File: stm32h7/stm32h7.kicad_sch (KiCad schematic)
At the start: 23 parts, among them J1 Conn_02x18_Counter_Clockwise, J2 Conn_02x18_Counter_Clockwise, J3 Conn_02x18_Counter_Clockwise, J4 Conn_02x18_Counter_Clockwise, SW1 SW_SPDT, U1 STM32H743ZITx, Y1 ABM3-8.000MHZ

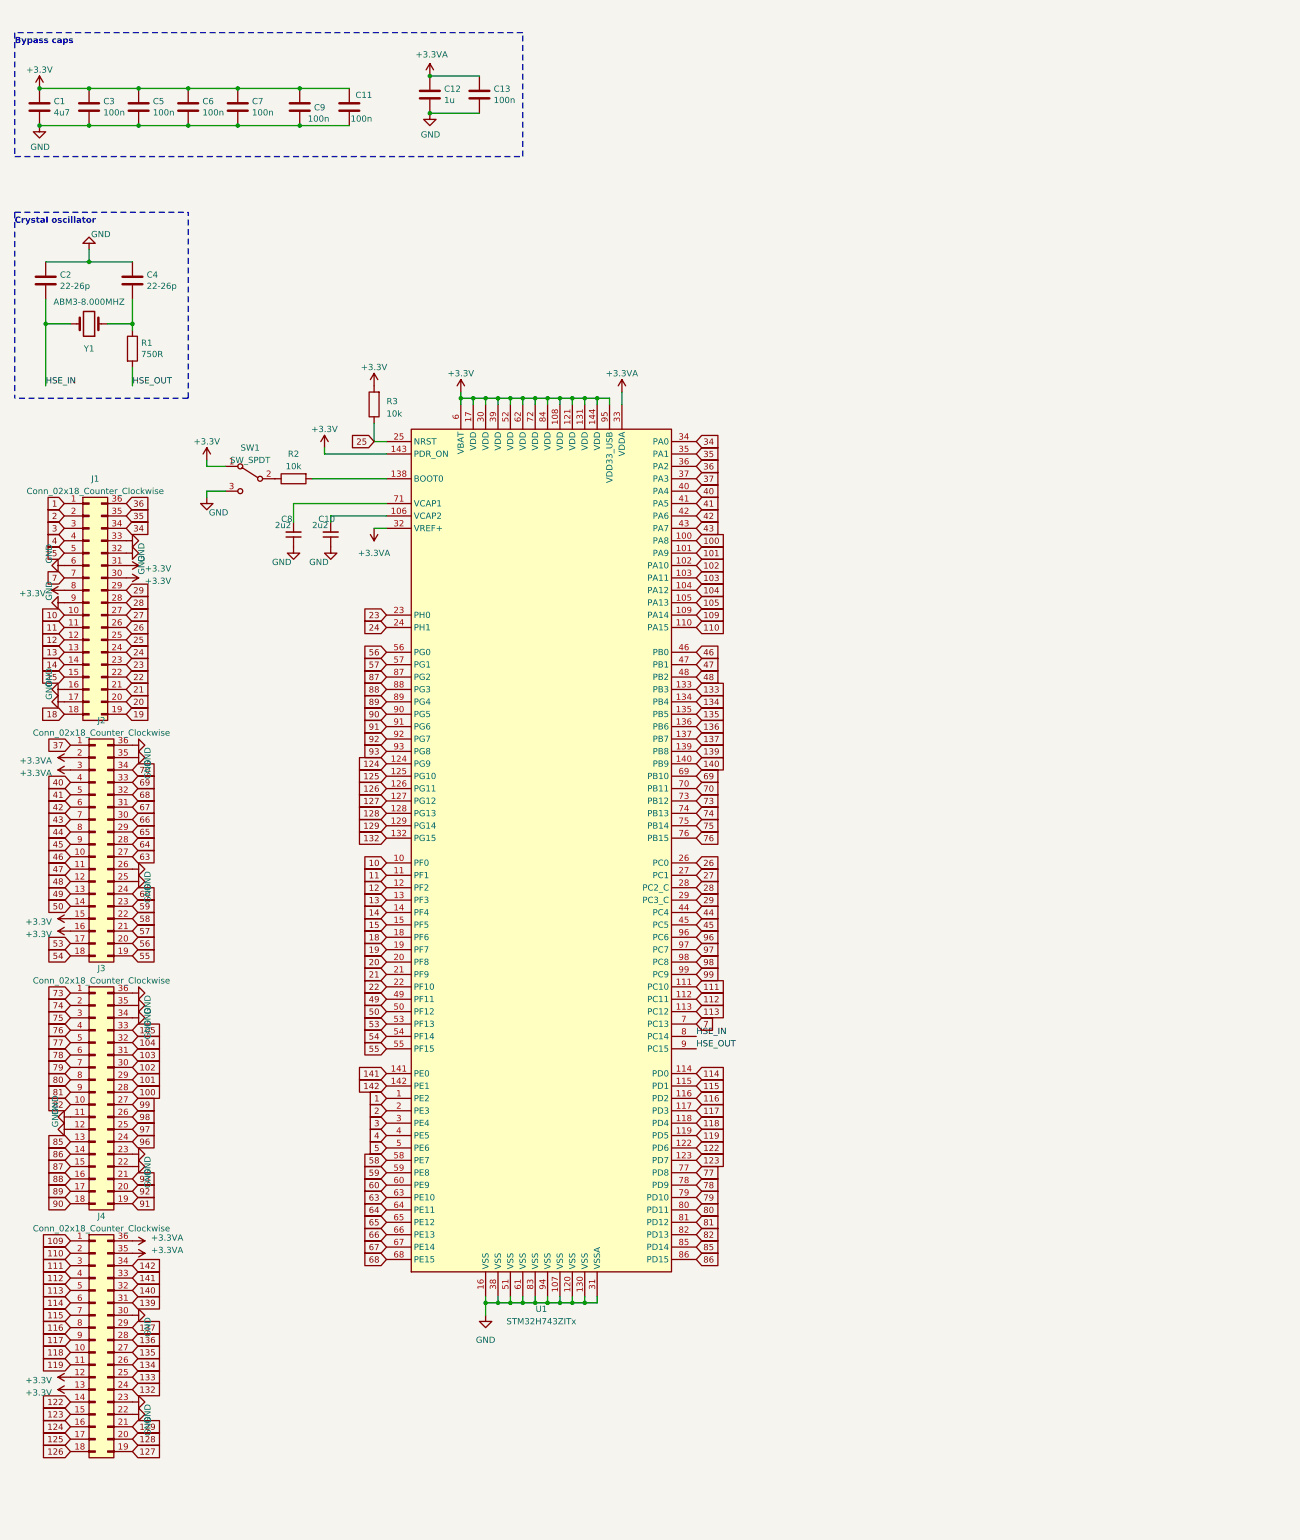
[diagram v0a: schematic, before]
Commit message: add gerber for stm32h7
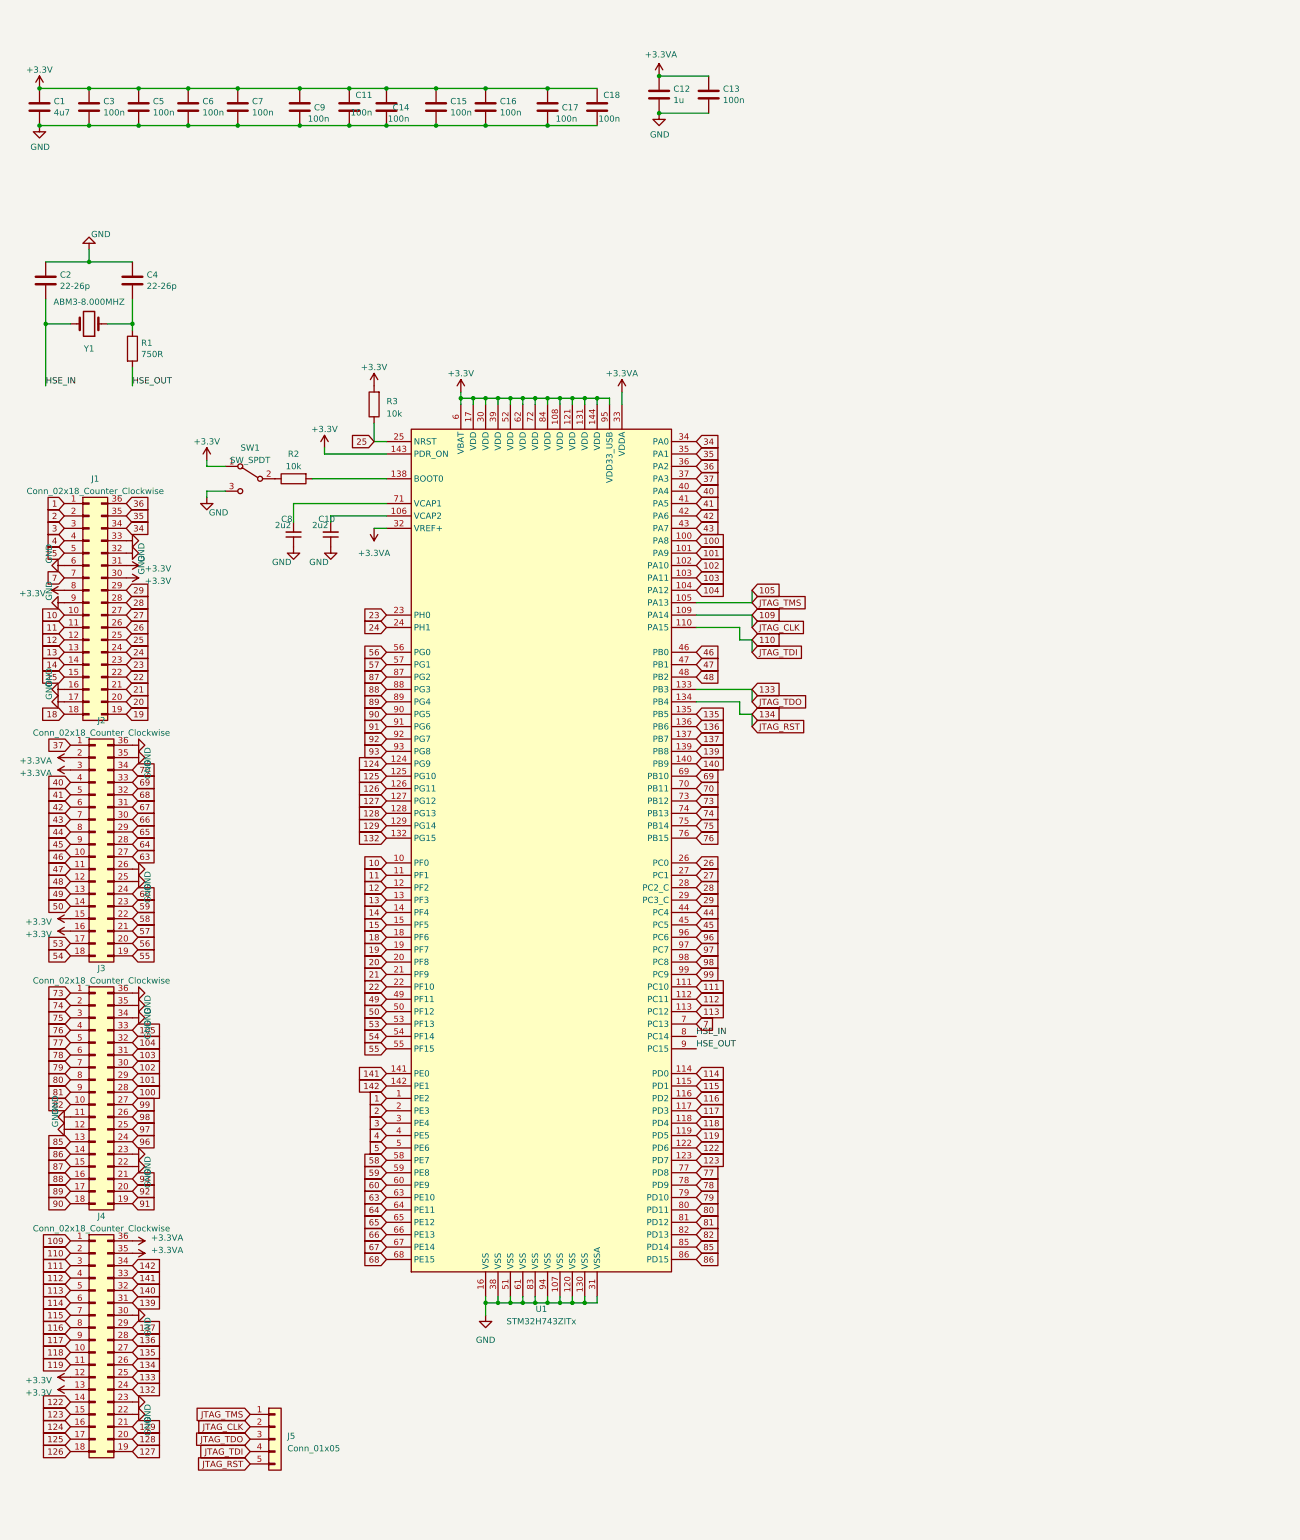
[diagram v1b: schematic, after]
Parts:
- added C14, C15, C16, C17, C18: 100n, Capacitor_SMD:C_0603_1608Metric, symbol Device:C
- added J5: Conn_01x05, Connector_PinHeader_2.00mm:PinHeader_1x05_P2.00mm_Vertical, symbol Connector_Generic:Conn_01x05
- C10, C8: LCSC (none) -> C23630; LCSC Part # (none) -> C23630
- R2, R3: LCSC (none) -> C25804; LCSC Part # (none) -> C25804
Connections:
- net +3V3: now also C14.1, C15.1, C16.1, C17.1, C18.1
- net 105: now also J5.1 (Pin_1)
- net 109: now also J5.2 (Pin_2)
- net 110: now also J5.4 (Pin_4)
- net 133: now also J5.3 (Pin_3)
- net 134: now also J5.5 (Pin_5)
- net GND: now also C14.2, C15.2, C16.2, C17.2, C18.2
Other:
- note removed: "Bypass caps"
- note removed: "Crystal oscillator"
- moved on the sheet: C12, C13

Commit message: add dedicated symbol and footprint for easier porting
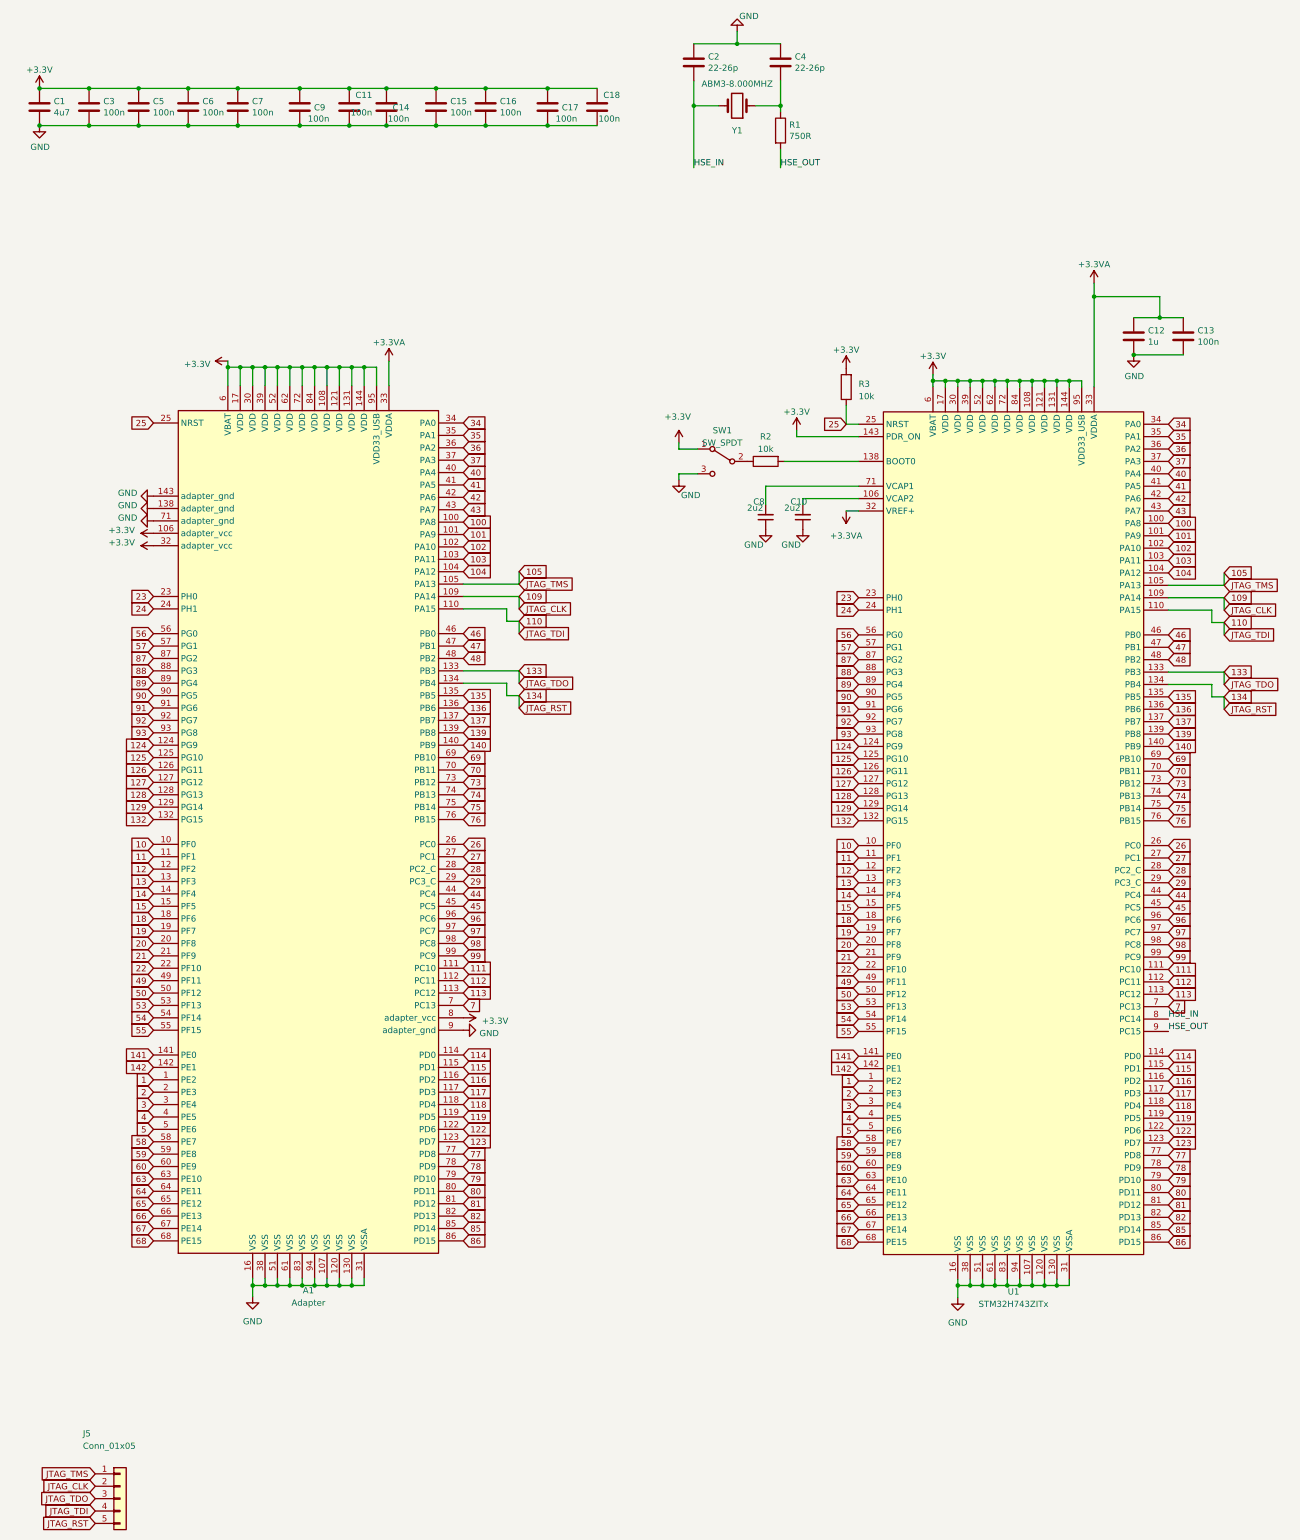
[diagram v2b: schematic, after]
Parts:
- removed J1, J2, J3, J4: Conn_02x18_Counter_Clockwise, Connector_PinHeader_2.00mm:PinHeader_2x18_P2.00mm_Vertical, symbol Connector_Generic:Conn_02x18_Counter_Clockwise
- added A1: Adapter, Connector_PinHeader_2.00mm:stm32h7_adapter, symbol MCU_ST_STM32H7:STM32H743ZITx
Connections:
- net +3.3VA: now also A1.33 (VDDA)
- net +3V3: now also A1.106 (adapter_vcc), A1.108 (VDD), A1.121 (VDD), A1.131 (VDD), A1.144 (VDD), A1.17 (VDD), A1.30 (VDD), A1.32 (adapter_vcc), A1.39 (VDD), A1.52 (VDD), A1.6 (VBAT), A1.62 (VDD), A1.72 (VDD), A1.8 (adapter_vcc), A1.84 (VDD), A1.95 (VDD33_USB)
- net 1: now also A1.1 (PE2)
- net 10: now also A1.10 (PF0)
- net 100: now also A1.100 (PA8)
- net 101: now also A1.101 (PA9)
- net 102: now also A1.102 (PA10)
- net 103: now also A1.103 (PA11)
- net 104: now also A1.104 (PA12)
- net 105: now also A1.105 (PA13)
- net 109: now also A1.109 (PA14)
- net 11: now also A1.11 (PF1)
- net 110: now also A1.110 (PA15)
- net 111: now also A1.111 (PC10)
- net 112: now also A1.112 (PC11)
- net 113: now also A1.113 (PC12)
- net 114: now also A1.114 (PD0)
- net 115: now also A1.115 (PD1)
- net 116: now also A1.116 (PD2)
- net 117: now also A1.117 (PD3)
- net 118: now also A1.118 (PD4)
- net 119: now also A1.119 (PD5)
- net 12: now also A1.12 (PF2)
- net 122: now also A1.122 (PD6)
- net 123: now also A1.123 (PD7)
- net 124: now also A1.124 (PG9)
- net 125: now also A1.125 (PG10)
- net 126: now also A1.126 (PG11)
- net 127: now also A1.127 (PG12)
- net 128: now also A1.128 (PG13)
- net 129: now also A1.129 (PG14)
- net 13: now also A1.13 (PF3)
- net 132: now also A1.132 (PG15)
- net 133: now also A1.133 (PB3)
- net 134: now also A1.134 (PB4)
- net 135: now also A1.135 (PB5)
- net 136: now also A1.136 (PB6)
- net 137: now also A1.137 (PB7)
- net 139: now also A1.139 (PB8)
- net 14: now also A1.14 (PF4)
- net 140: now also A1.140 (PB9)
- net 141: now also A1.141 (PE0)
- net 142: now also A1.142 (PE1)
- net 15: now also A1.15 (PF5)
- net 18: now also A1.18 (PF6)
- net 19: now also A1.19 (PF7)
- net 2: now also A1.2 (PE3)
- net 20: now also A1.20 (PF8)
- net 21: now also A1.21 (PF9)
- net 22: now also A1.22 (PF10)
- net 23: now also A1.23 (PH0)
- net 24: now also A1.24 (PH1)
- net 25: now also A1.25 (NRST)
- net 26: now also A1.26 (PC0)
- net 27: now also A1.27 (PC1)
- net 28: now also A1.28 (PC2_C)
- net 29: now also A1.29 (PC3_C)
- net 3: now also A1.3 (PE4)
- net 34: now also A1.34 (PA0)
- net 35: now also A1.35 (PA1)
- net 36: now also A1.36 (PA2)
- net 37: now also A1.37 (PA3)
- net 4: now also A1.4 (PE5)
- net 40: now also A1.40 (PA4)
- net 41: now also A1.41 (PA5)
- net 42: now also A1.42 (PA6)
- net 43: now also A1.43 (PA7)
- net 44: now also A1.44 (PC4)
- net 45: now also A1.45 (PC5)
- net 46: now also A1.46 (PB0)
- net 47: now also A1.47 (PB1)
- net 48: now also A1.48 (PB2)
- net 49: now also A1.49 (PF11)
- net 5: now also A1.5 (PE6)
- net 50: now also A1.50 (PF12)
- net 53: now also A1.53 (PF13)
- net 54: now also A1.54 (PF14)
- net 55: now also A1.55 (PF15)
- net 56: now also A1.56 (PG0)
- net 57: now also A1.57 (PG1)
- net 58: now also A1.58 (PE7)
- net 59: now also A1.59 (PE8)
- net 60: now also A1.60 (PE9)
- net 63: now also A1.63 (PE10)
- net 64: now also A1.64 (PE11)
- net 65: now also A1.65 (PE12)
- net 66: now also A1.66 (PE13)
- net 67: now also A1.67 (PE14)
- net 68: now also A1.68 (PE15)
- net 69: now also A1.69 (PB10)
- net 7: now also A1.7 (PC13)
- net 70: now also A1.70 (PB11)
- net 73: now also A1.73 (PB12)
- net 74: now also A1.74 (PB13)
- net 75: now also A1.75 (PB14)
- net 76: now also A1.76 (PB15)
- net 77: now also A1.77 (PD8)
- net 78: now also A1.78 (PD9)
- net 79: now also A1.79 (PD10)
- net 80: now also A1.80 (PD11)
- net 81: now also A1.81 (PD12)
- net 82: now also A1.82 (PD13)
- net 85: now also A1.85 (PD14)
- net 86: now also A1.86 (PD15)
- net 87: now also A1.87 (PG2)
- net 88: now also A1.88 (PG3)
- net 89: now also A1.89 (PG4)
- net 90: now also A1.90 (PG5)
- net 91: now also A1.91 (PG6)
- net 92: now also A1.92 (PG7)
- net 93: now also A1.93 (PG8)
- net 96: now also A1.96 (PC6)
- net 97: now also A1.97 (PC7)
- net 98: now also A1.98 (PC8)
- net 99: now also A1.99 (PC9)
- net GND: now also A1.107 (VSS), A1.120 (VSS), A1.130 (VSS), A1.138 (adapter_gnd), A1.143 (adapter_gnd), A1.16 (VSS), A1.31 (VSSA), A1.38 (VSS), A1.51 (VSS), A1.61 (VSS), A1.71 (adapter_gnd), A1.83 (VSS), A1.9 (adapter_gnd), A1.94 (VSS)
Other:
- moved on the sheet: C10, C12, C13, C2, C4, C8, J5, R1, R2, R3, SW1, U1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

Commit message: update stm32h7 adapter
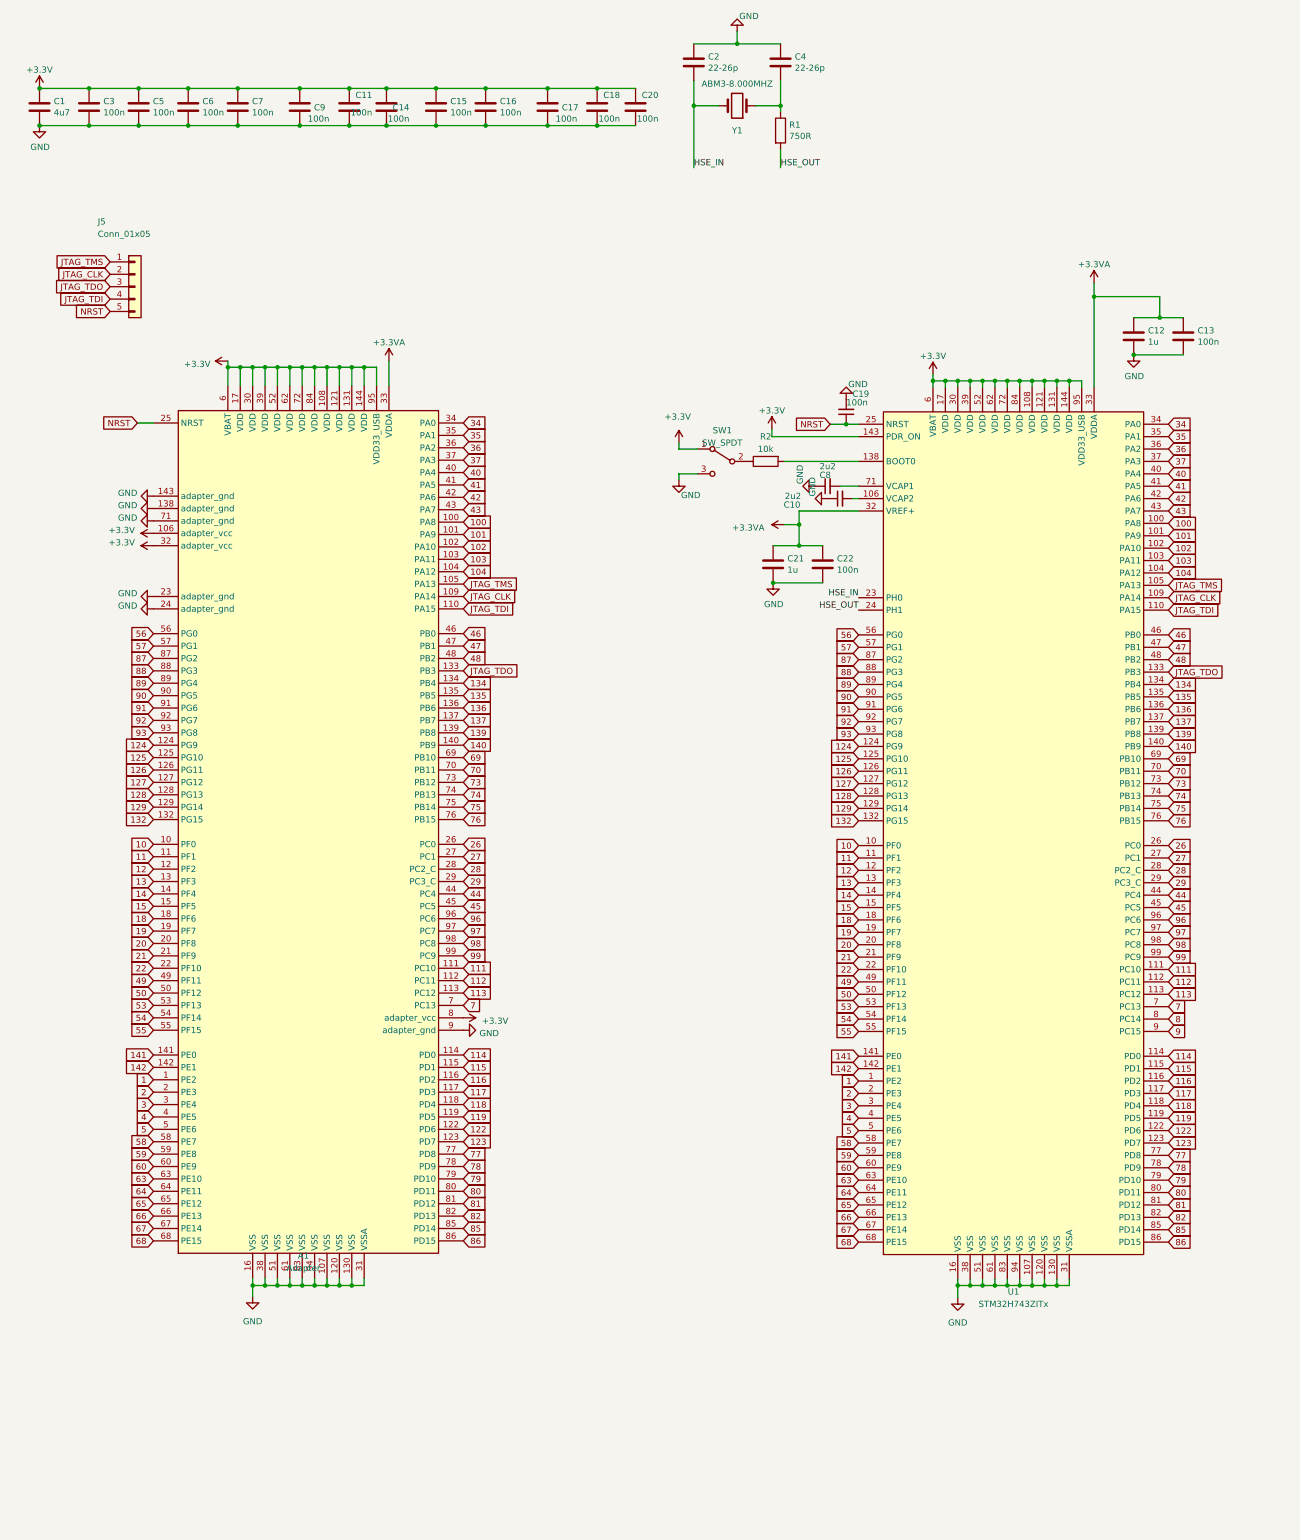
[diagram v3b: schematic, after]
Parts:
- removed R3: 10k, Resistor_SMD:R_0603_1608Metric, symbol Device:R
- added C19: 100n, Capacitor_SMD:C_0603_1608Metric, symbol Device:C_Small
- added C20, C22: 100n, Capacitor_SMD:C_0603_1608Metric, symbol Device:C
- added C21: 1u, Capacitor_SMD:C_0603_1608Metric, symbol Device:C
- A1: symbol MCU_ST_STM32H7:STM32H743ZITx -> adapters:stm32h7_144_adapter
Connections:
- net +3.3VA: now also C21.1, C22.1
- net +3V3: now also C20.1
- net 134: no longer J5.5 (Pin_5)
- net GND: now also A1.23 (adapter_gnd), A1.24 (adapter_gnd), C19.2, C20.2, C21.2, C22.2
- net HSE_IN: now also U1.23 (PH0); no longer U1.8 (PC14)
- net HSE_OUT: now also U1.24 (PH1); no longer U1.9 (PC15)
- net 105 renamed JTAG_TMS
- net 109 renamed JTAG_CLK
- net 110 renamed JTAG_TDI
- net 133 renamed JTAG_TDO
- removed net 23: A1.23 (PH0), U1.23 (PH0)
- removed net 24: A1.24 (PH1), U1.24 (PH1)
- net 25 renamed NRST
- net NRST: now also J5.5 (Pin_5), C19.1
- new net 8: U1.8 (PC14)
- new net 9: U1.9 (PC15)
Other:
- moved on the sheet: C10, C8, J5
